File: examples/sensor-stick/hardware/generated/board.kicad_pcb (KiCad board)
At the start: 2 copper layers, 26 x 76 mm, 27 parts, among them J1 USB_C_Receptacle_HRO_TYPE-C-3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, U1 QFN-56-1EP_7x7mm_P0.4mm_EP3.2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, U2 SOIC-8_5.23x5.23mm_P1.27mm, U3 SOT-223-3_L6.5-W3.4-P2.30-LS7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, U4 SENSOR-SMD_L3.0-W3.0-P1.00-BR, Y1 Crystal_SMD_3225-4Pin_3.2x2.5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

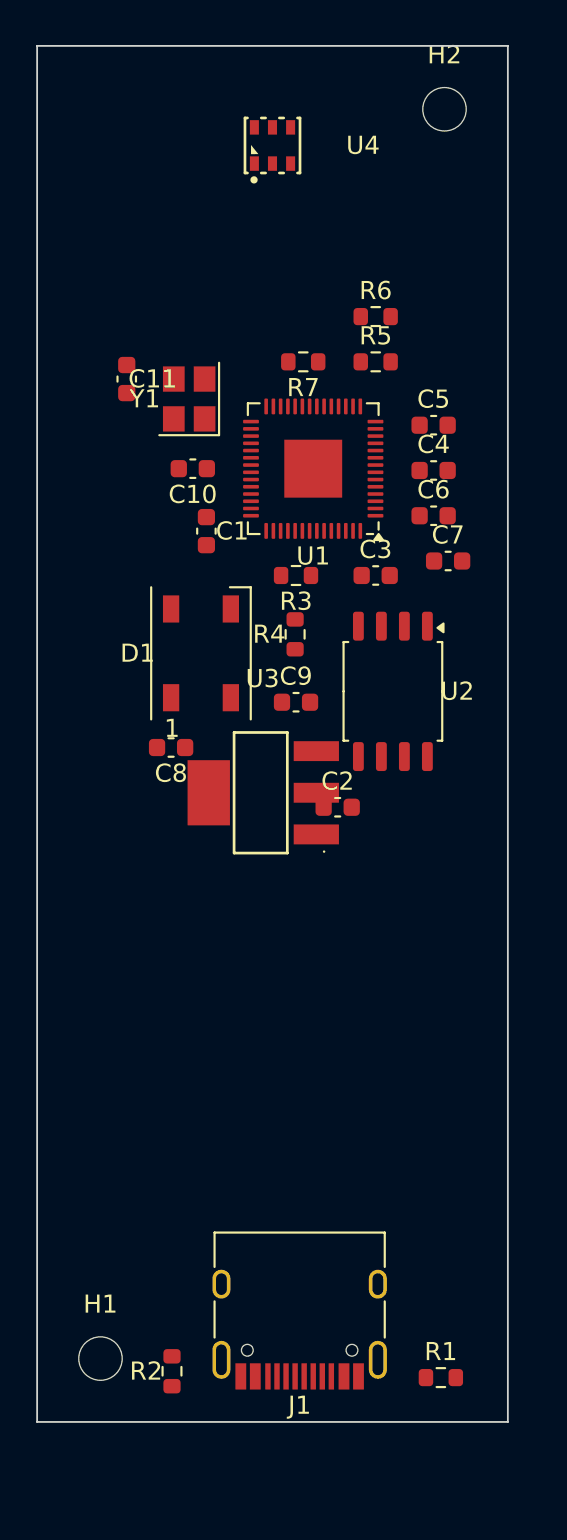
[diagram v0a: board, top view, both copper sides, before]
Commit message: feat(examples): sensor-stick in blue, every part a real model, rebuilt
- case.colour = blue; nothing of any other product's look
- the regulator from KiCad's own library (flattened `extends`), the
  sensor and flash from LCSC's library with their models, the USB-C
  socket on KiCad's land pattern with LCSC's model, measured onto its
  drilled holes; the socket's mouth now faces the wall (it faced in)
- routed, DRC clean, every fit check passing, every part orderable
- the guide rebuilds it from scratch; its case study records each
  refusal of the first build, and the one no gate caught

Co-Authored-By: Claude Opus 5.5 <noreply@anthropic.com>
Claude-Session: https://claude.ai/code/session_01F145W5B7sgzWKAnWcVES4m
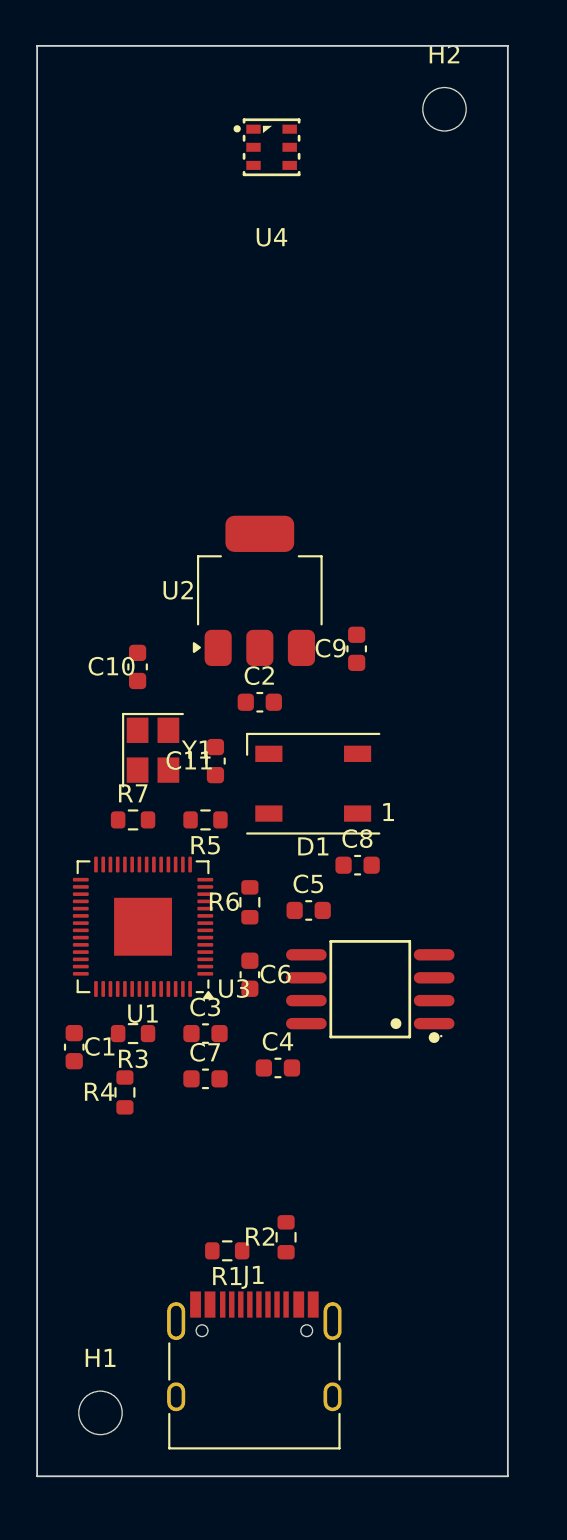
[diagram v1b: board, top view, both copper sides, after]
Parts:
- U2: value SOIC-8_5.23x5.23mm_P1.27mm -> SOT-223-3_TabPin2; footprint Package_SO:SOIC-8_5.23x5.23mm_P1.27mm -> Package_TO_SOT_SMD:SOT-223-3_TabPin2
- U3: value SOT-223-3_L6.5-W3.4-P2.30-LS7.0-BR -> SOIC-8_L5.3-W5.3-P1.27-LS8.0-BL; footprint lcsc:SOT-223-3_L6.5-W3.4-P2.30-LS7.0-BR -> lcsc:SOIC-8_L5.3-W5.3-P1.27-LS8.0-BL
- moved C4 34.1 mm to (113.3, 156.4)
- moved R6 33.1 mm to (111.8, 147.3), turned to 90 degrees
- moved C7 31.6 mm to (109.3, 157.1)
- moved C1 29.4 mm to (102.0, 155.3)
- moved C5 27.7 mm to (115.0, 147.8)
- moved C6 27.3 mm to (111.8, 151.3), turned to 270 degrees
- moved C3 27.0 mm to (109.3, 154.6)
- moved R4 27.0 mm to (104.8, 157.8)
- moved U1 27.0 mm to (105.8, 148.7)
- moved R5 27.0 mm to (109.3, 142.8), turned to 180 degrees
- moved R7 27.0 mm to (105.3, 142.8), turned to 0 degrees
- moved R3 26.9 mm to (105.3, 154.6)
- moved C11 21.7 mm to (109.8, 139.5), turned to 90 degrees
- moved Y1 19.5 mm to (106.4, 138.9), turned to 270 degrees
- moved R1 13.7 mm to (110.5, 166.6), turned to 180 degrees
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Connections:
- U2 pad 1: QSPI_SS -> GND
- U2 pad 2: QSPI_SD1 -> 3V3
- U2 pad 3: QSPI_SD2 -> VBUS
- U3 pad 1: GND -> QSPI_SS
- U3 pad 2: 3V3 -> QSPI_SD1
- U3 pad 3: VBUS -> QSPI_SD2
- U3 pad 4: 3V3 -> GND
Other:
- board size 26 x 76 mm -> 26 x 79 mm

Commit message: feat(examples): sensor-stick's USB-C socket flush with the case
The socket's mouth is 0.79 mm in from the case's face, in a notch of its
face plus 1 mm that the lid closes. The plug end's chamfer is smaller and
the floor search steps 0.5 mm, so the board can stand against that wall.
Rebuilt: routed, DRC clean, every check passing. The guide's case study
gains the six things this found.

Co-Authored-By: Claude Opus 5.5 <noreply@anthropic.com>
Claude-Session: https://claude.ai/code/session_01F145W5B7sgzWKAnWcVES4m
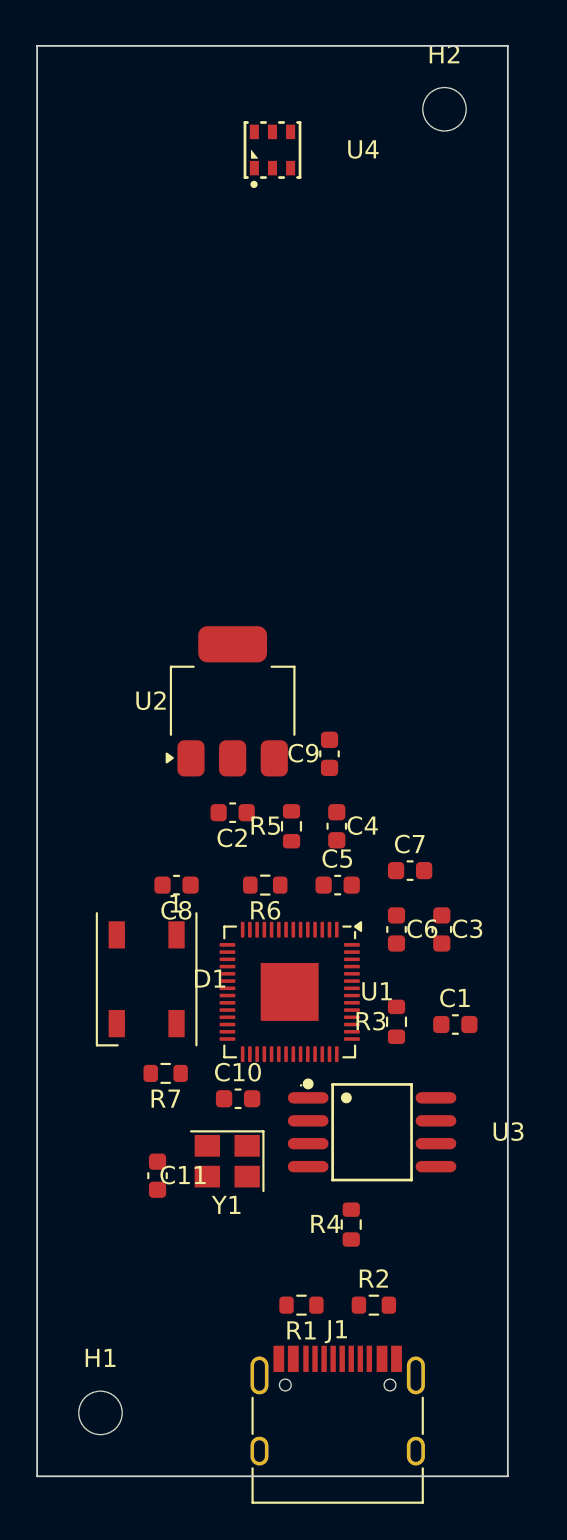
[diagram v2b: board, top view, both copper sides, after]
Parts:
- moved C10 24.5 mm to (111.1, 158.2), turned to 0 degrees
- moved C11 23.1 mm to (106.7, 162.4), turned to 270 degrees
- moved Y1 23.1 mm to (110.5, 161.6), turned to 180 degrees
- moved C1 21.1 mm to (123.1, 154.1), turned to 0 degrees
- moved C7 16.1 mm to (120.6, 145.6)
- moved R3 14.6 mm to (119.8, 153.9), turned to 90 degrees
- moved R4 14.5 mm to (117.3, 165.1)
- moved C3 14.3 mm to (122.3, 148.8), turned to 270 degrees
- moved D1 14.2 mm to (106.0, 151.6), turned to 270 degrees
- moved R7 14.1 mm to (107.1, 156.8), turned to 180 degrees
- moved C4 13.7 mm to (116.5, 143.1), turned to 270 degrees
- moved C8 10.1 mm to (107.7, 146.3), turned to 180 degrees
- moved U1 8.86 mm to (114.0, 152.2), turned to 270 degrees
- moved C6 8.48 mm to (119.8, 148.8)
- moved U3 7.90 mm to (118.5, 160.0), turned to 270 degrees
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
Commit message: feat(hardware): place the case floor by solver, not by search (P2)
Sockets (either way round) and the board are a second placement model,
floor-model.json -> floor.json, solved by the same place.py. The cavity
can be any outline, so fid computes per item and turn the rectangles its
centre fits in (half-millimetre rows, a tenth where they change, ends
bisected to a hundredth) and the solver chooses among them. Two generic
additions: `inside` as per-turn centre rectangles, and `near` with slack
(cover a point, not centre on it). Obstacles need not clear each other.

The bounded search is deleted; case.grid_mm no longer touches the floor.
Answers are checked against the exact fit. The sensor stick's board now
stands at its exact limit without its grid_mm workaround (mouth 0.69 mm
from the face, was 0.79). A part that fits nowhere, and two that fit
apart but not together, fail naming them.

Co-Authored-By: Claude Opus 5.5 <noreply@anthropic.com>
Claude-Session: https://claude.ai/code/session_01F145W5B7sgzWKAnWcVES4m
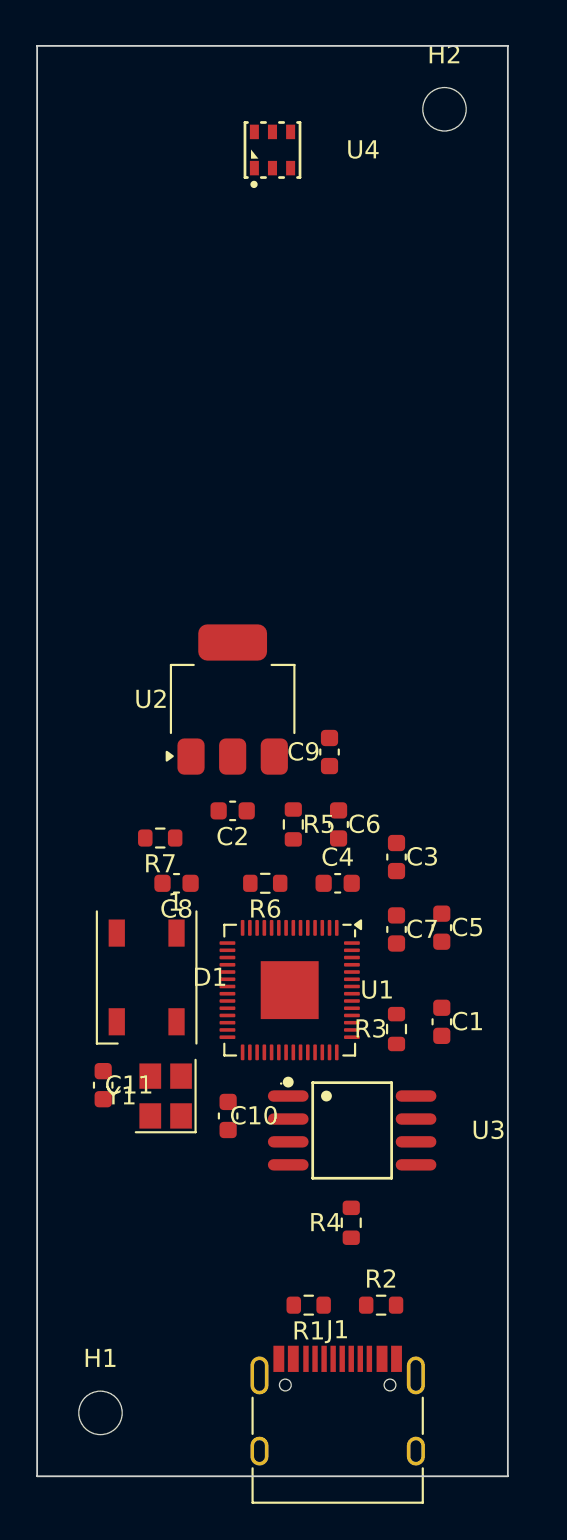
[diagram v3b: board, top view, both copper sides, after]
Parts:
- moved R7 13.0 mm to (106.8, 143.8)
- moved C6 6.62 mm to (116.7, 143.0)
- moved C5 6.21 mm to (122.3, 148.7), turned to 270 degrees
- moved C11 5.83 mm to (103.7, 157.4)
- moved Y1 4.95 mm to (107.1, 158.0), turned to 90 degrees
- moved C3 4.72 mm to (119.8, 144.8)
- moved C7 3.34 mm to (119.8, 148.8), turned to 270 degrees
- moved C4 3.15 mm to (116.6, 146.2), turned to 0 degrees
- moved U3 1.10 mm to (117.4, 159.9)
- moved C10 1.10 mm to (110.5, 159.1), turned to 270 degrees
- moved C1 0.76 mm to (122.3, 153.9), turned to 270 degrees
- moved R1 0.40 mm to (115.0, 169.6)
- moved R2 0.40 mm to (119.0, 169.6)
- moved R3 0.40 mm to (119.8, 154.3)
- moved R5 0.14 mm to (114.2, 143.0), turned to 270 degrees
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
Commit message: fix(examples): buffer the sensor stick's LED data line to 5 V
The WS2812B on 5 V reads high only above 0.7 x VDD = 3.5 V, and the
RP2040 drives 3.3 V: out of spec, though it often works on a bench. A
74AHCT1G125 on 5 V (TTL input, 2.0 V high) sits between them, with its
own decoupling; the MCU side keeps the LED_DIN net, so the firmware is
unchanged. No gate compares output levels with input thresholds, so the
case study gains a row: four of twenty-four caught only by review.

The board stays 26 x 79 mm at fill 0.66 and routes first time. Prices
now come from LCSC: $4.74 of parts per board at five. Renders refreshed.

Co-Authored-By: Claude Opus 5.5 <noreply@anthropic.com>
Claude-Session: https://claude.ai/code/session_01F145W5B7sgzWKAnWcVES4m
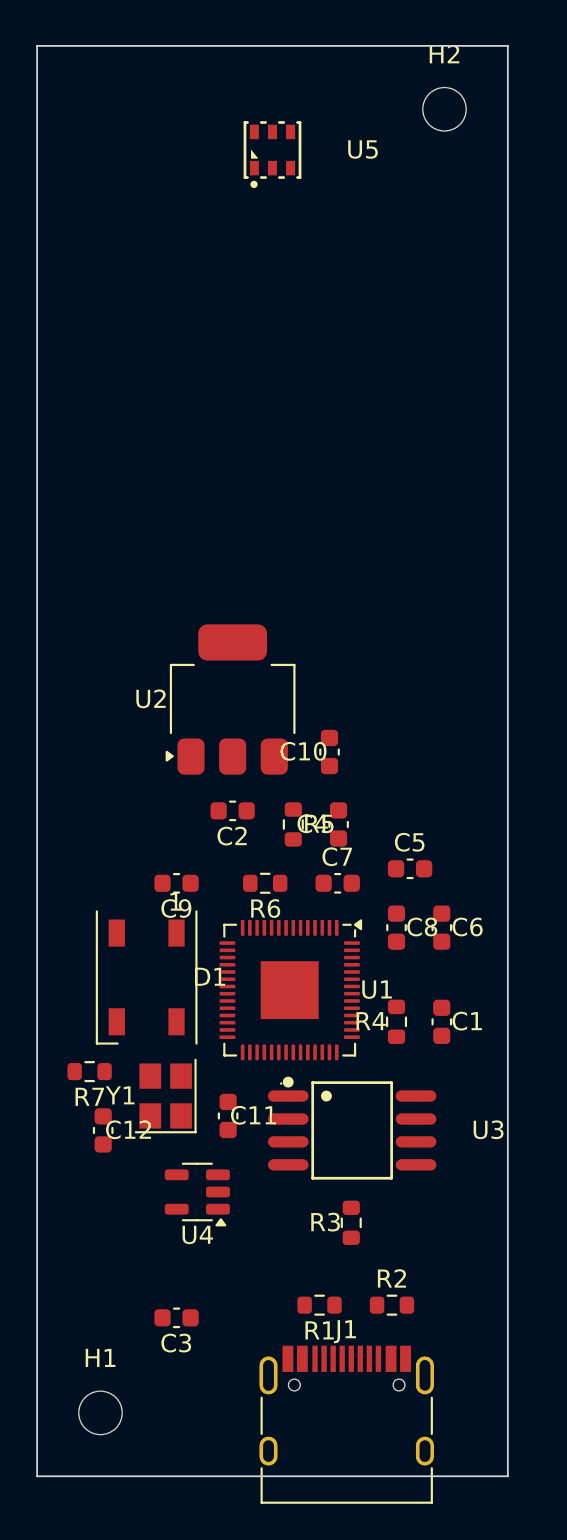
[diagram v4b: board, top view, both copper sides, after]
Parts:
- added C12: C_0603_1608Metric, Capacitor_SMD:C_0603_1608Metric, F.Cu at (103.7, 159.9)
- added U5: SENSOR-SMD_L3.0-W3.0-P1.00-BR, lcsc:SENSOR-SMD_L3.0-W3.0-P1.00-BR, F.Cu at (113.0, 105.8)
- U4: value SENSOR-SMD_L3.0-W3.0-P1.00-BR -> SOT-23-5; footprint lcsc:SENSOR-SMD_L3.0-W3.0-P1.00-BR -> Package_TO_SOT_SMD:SOT-23-5
- moved U4 57.7 mm to (108.8, 163.3), turned to 180 degrees
- moved C3 28.2 mm to (107.7, 170.2), turned to 180 degrees
- moved C10 20.9 mm to (116.2, 139.0), turned to 90 degrees
- moved R7 13.5 mm to (102.9, 156.7)
- moved C8 12.4 mm to (119.8, 148.7), turned to 270 degrees
- moved R4 11.4 mm to (119.8, 153.9)
- moved C9 11.1 mm to (107.7, 146.2), turned to 180 degrees
- moved R3 11.0 mm to (117.3, 165.0)
- moved C6 8.06 mm to (122.3, 148.7)
- moved C11 7.11 mm to (110.5, 159.1)
- moved C7 4.13 mm to (116.6, 146.2), turned to 0 degrees
- moved C5 3.69 mm to (120.6, 145.4), turned to 0 degrees
- moved C4 3.25 mm to (116.7, 143.0), turned to 90 degrees
- moved R1 0.60 mm to (115.6, 169.6)
- moved R2 0.60 mm to (119.6, 169.6)
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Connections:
- C10 pad 1: XIN -> VBUS
- C11 pad 1: XOUT_X -> XIN
- C3 pad 1: 3V3 -> VBUS
- C8 pad 1: VBUS -> 3V3
- D1 pad 4: LED_DIN -> LED_DIN_5V
- U4 pad 1: (no net) -> GND
- U4 pad 2: 3V3 -> LED_DIN
- U4 pad 3: SENSOR_SCL -> GND
- U4 pad 4: SENSOR_SDA -> LED_DIN_5V
- U4 pad 5: GND -> VBUS

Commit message: feat(hardware): cut the board to its case; fix two sealed-vent bugs
board.cut_mm lets a board keep its length where the case narrows and
lose its corners instead: the outline is the rectangle clipped to the
cavity (wall and clearance in), written to Edge.Cuts as a polygon. The
floor fits the cut shape, cut corners are obstacles named in conflicts,
default holes move in, and the case, the routing edge strip, the
ratsnest and the insertion check all use the outline. The sensor
stick's plug-end chamfer is back at full size; its board loses two
corners, not its length.

Found by building the private reference product on this release:
- a vent sealed to a board part was sized by its chimney ring inside
  its lid mark, holding a vent in a small mark away from where the
  ring had room. The vent's own body now takes the nearest spot whose
  ring fits the cavity below.
- the floor treated the board's reach under a sealed vent as a
  preference. The board's centre is now held where the ring can land
  on it within the chimney's lean.
- cad.py crashed on solids whose boxes overlap and bodies do not:
  build123d returns None for an empty intersection.

Co-Authored-By: Claude Opus 5.5 <noreply@anthropic.com>
Claude-Session: https://claude.ai/code/session_01F145W5B7sgzWKAnWcVES4m
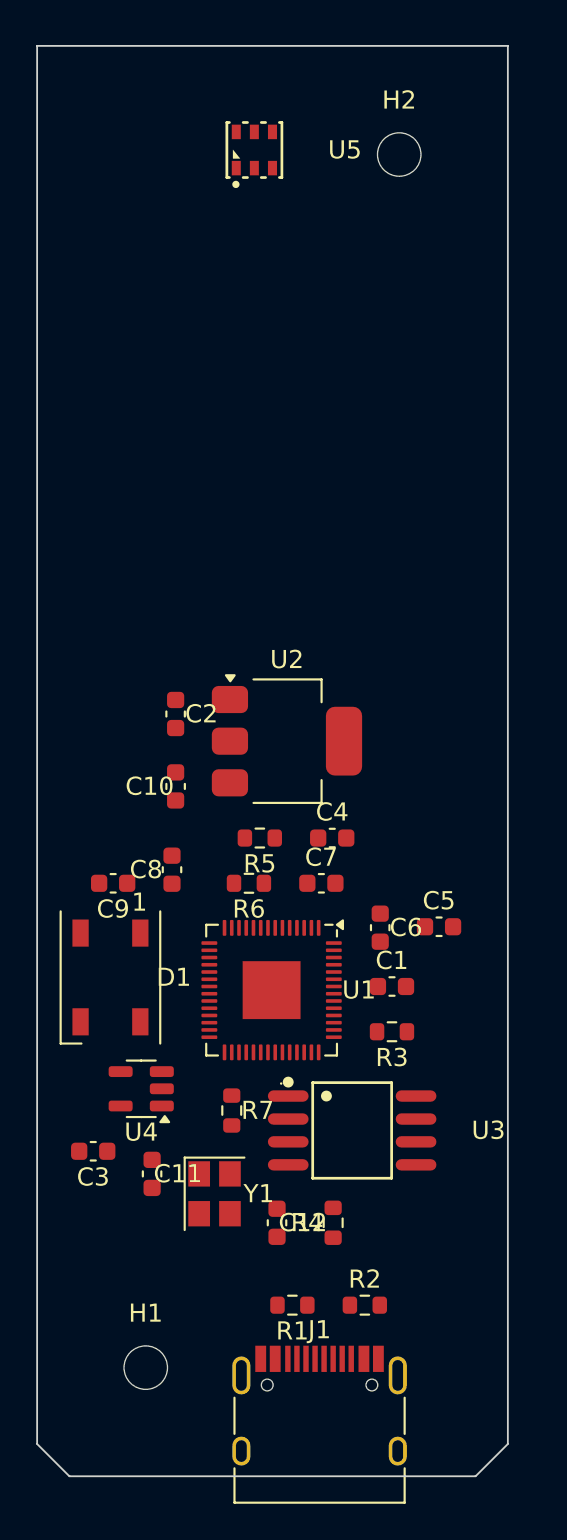
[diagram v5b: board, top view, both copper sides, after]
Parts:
- moved C8 12.8 mm to (107.5, 145.5), turned to 90 degrees
- moved R4 11.6 mm to (116.3, 165.0)
- moved C12 10.9 mm to (113.2, 165.0)
- moved R3 10.8 mm to (119.6, 154.4), turned to 180 degrees
- moved C3 10.3 mm to (103.1, 161.1)
- moved C10 8.71 mm to (107.7, 140.9)
- moved R7 8.14 mm to (110.8, 158.8), turned to 270 degrees
- moved U4 6.49 mm to (105.8, 157.6)
- moved C2 6.21 mm to (107.7, 136.9), turned to 270 degrees
- moved Y1 6.04 mm to (109.8, 163.4), turned to 270 degrees
- moved C11 5.28 mm to (106.3, 162.3)
- moved U2 3.78 mm to (113.8, 138.4), turned to 0 degrees
- moved C5 3.58 mm to (122.2, 148.7)
- moved H1 3.54 mm to (106.0, 173.0)
- moved H2 3.54 mm to (120.0, 106.0)
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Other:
- outline, holes or cut-outs redrawn
